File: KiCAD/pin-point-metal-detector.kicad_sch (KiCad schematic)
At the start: 19 parts, among them J1 batt. con., J2 circuit con., SW1 Power, Y1 12Mhz

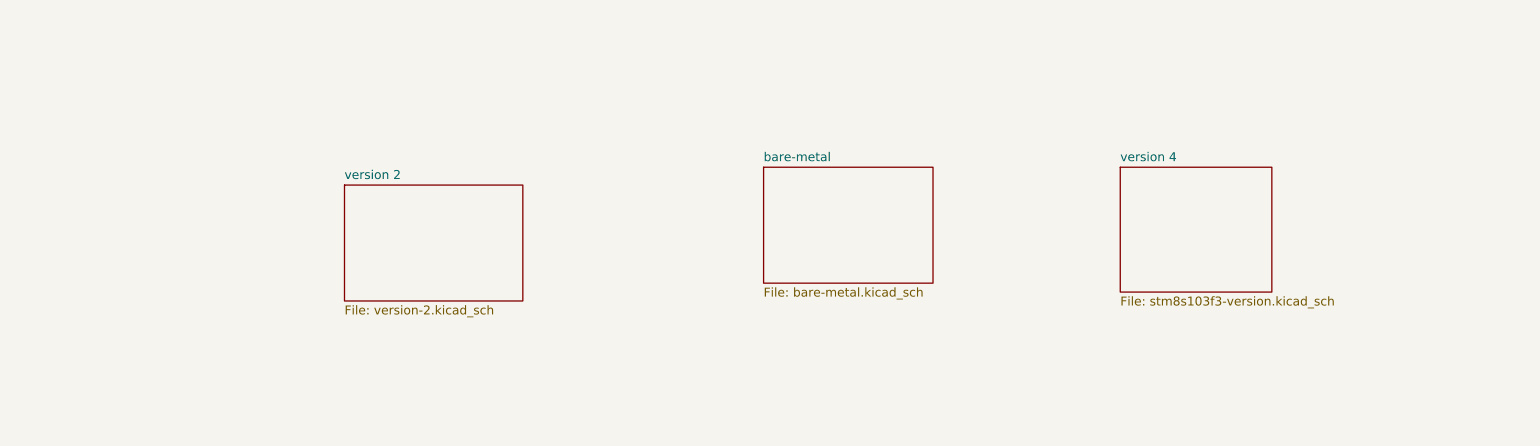
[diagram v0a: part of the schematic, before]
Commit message: New design and new software in bare-metal. Best result up to now
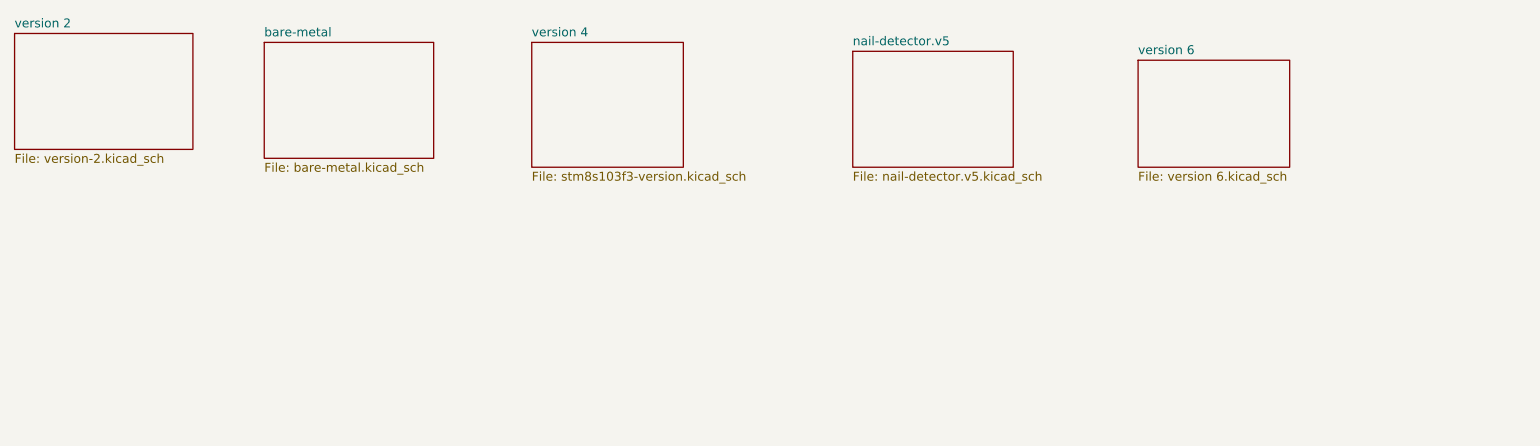
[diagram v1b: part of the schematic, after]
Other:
- added sheet nail-detector.v5 (nail-detector.v5.kicad_sch)
- added sheet version 6 (version 6.kicad_sch)
